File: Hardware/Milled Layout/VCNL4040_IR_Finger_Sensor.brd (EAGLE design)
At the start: 20.4 x 17.8 mm, 9 parts, among them U1 VCNL4040

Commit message: Trace cleanup
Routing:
- net 3.3V: track 36.1 -> 34.6 mm
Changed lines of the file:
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@@
 <wire x1="14.859" y1="15.24" x2="15.24" y2="14.859" width="0.254" layer="1"/>
 <wire x1="15.24" y1="14.859" x2="15.24" y2="12.7" width="0.254" layer="1"/>
-<wire x1="5.93" y1="12.065" x2="5.93" y2="8.89" width="0.254" layer="1"/>
+<wire x1="5.93" y1="12.065" x2="5.93" y2="11.43" width="0.254" layer="1"/>
+<wire x1="5.93" y1="10.922" x2="5.93" y2="8.89" width="0.254" layer="1"/>
 <wire x1="5.93" y1="8.89" x2="5.93" y2="7.835" width="0.254" layer="1"/>
 <wire x1="4.23" y1="5.08" x2="4.23" y2="6.135" width="0.254" layer="1"/>
@@
 <wire x1="7.112" y1="3.683" x2="7.62" y2="3.175" width="0.254" layer="1"/>
 <wire x1="7.62" y1="3.175" x2="7.62" y2="1.27" width="0.254" layer="1"/>
-<wire x1="5.93" y1="8.89" x2="6.858" y2="8.89" width="0.254" layer="1"/>
-<wire x1="6.858" y1="8.89" x2="7.366" y2="9.398" width="0.254" layer="1"/>
-<wire x1="7.366" y1="9.398" x2="7.366" y2="10.541" width="0.254" layer="1"/>
-<wire x1="7.366" y1="10.541" x2="7.747" y2="10.922" width="0.254" layer="1"/>
-<wire x1="7.747" y1="10.922" x2="8.5475" y2="10.922" width="0.254" layer="1"/>
 <wire x1="8.5475" y1="10.922" x2="9.398" y2="10.922" width="0.254" layer="1"/>
 <wire x1="9.398" y1="10.922" x2="9.6225" y2="10.6975" width="0.254" layer="1"/>
 <wire x1="9.6225" y1="10.6975" x2="9.6225" y2="9.89" width="0.254" layer="1"/>
 <wire x1="8.5475" y1="9.89" x2="8.5475" y2="10.922" width="0.254" layer="1"/>
+<wire x1="8.5475" y1="10.922" x2="5.93" y2="10.922" width="0.254" layer="1"/>
+<wire x1="5.93" y1="10.922" x2="5.93" y2="11.43" width="0.254" layer="1"/>
 </signal>
 <signal name="N$1">

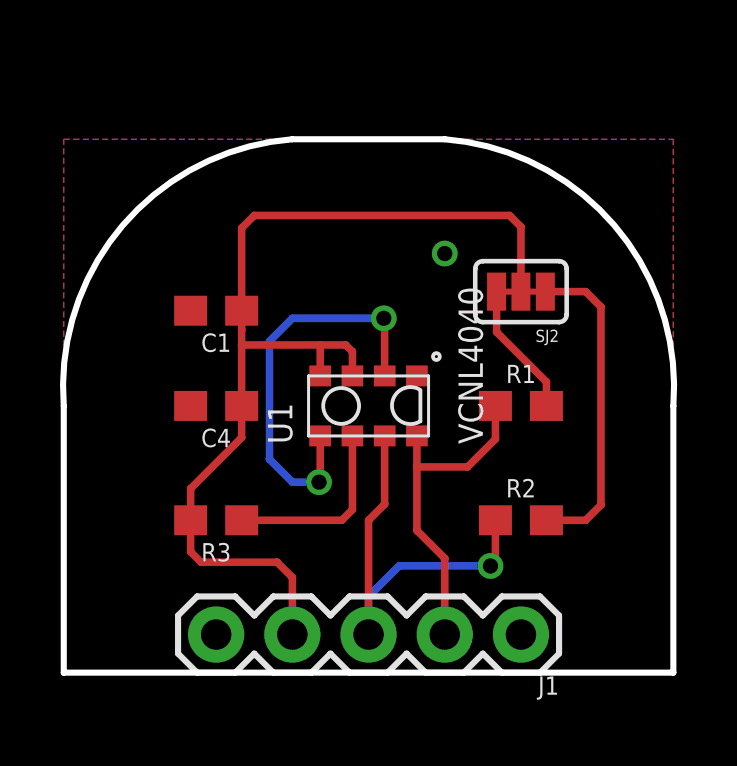
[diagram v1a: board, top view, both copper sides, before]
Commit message: Expanded bottom dimension to remove via
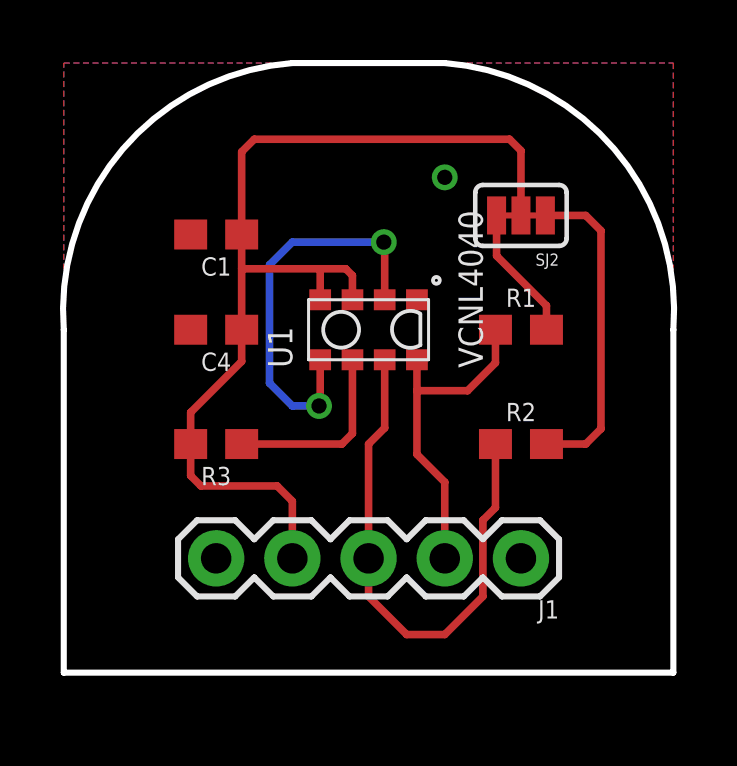
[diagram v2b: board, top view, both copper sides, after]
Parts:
- moved C1 2.54 mm to (5.08, 14.6)
- moved SJ2 2.54 mm to (15.2, 15.2)
- moved J1 2.54 mm to (15.2, 3.81)
- moved R2 2.54 mm to (15.2, 7.62)
- moved R3 2.54 mm to (5.08, 7.62)
- moved C4 2.54 mm to (5.08, 11.4)
- moved R1 2.54 mm to (15.2, 11.4)
- moved U1 2.54 mm to (10.2, 11.4)
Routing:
- net SDA: track 14.2 -> 18.2 mm, vias 1 -> 0
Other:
- board size 20.4 x 17.8 mm -> 20.4 x 20.3 mm
